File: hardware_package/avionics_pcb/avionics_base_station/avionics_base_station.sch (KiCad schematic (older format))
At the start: 3 parts, among them U1 NODEMCU, U2 RFM98

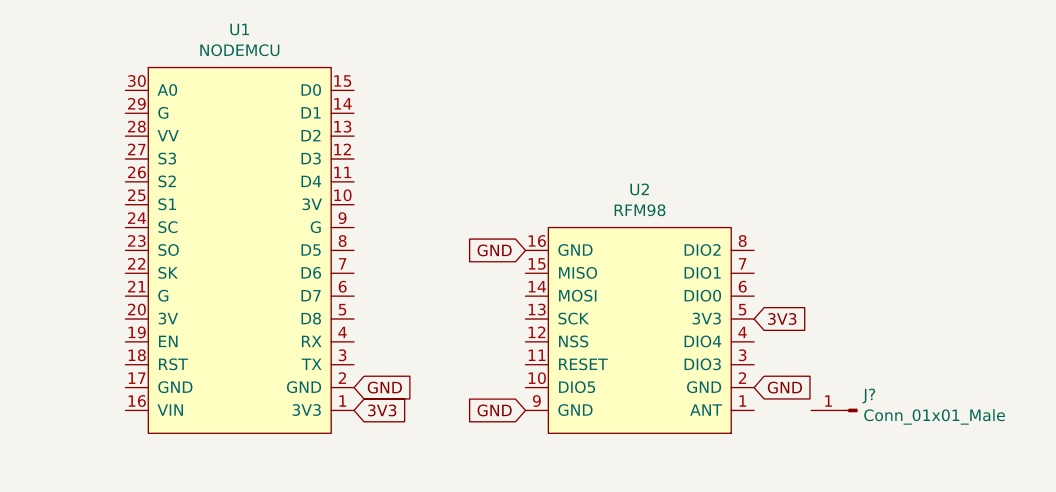
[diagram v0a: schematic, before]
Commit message: Completed the base station PCB
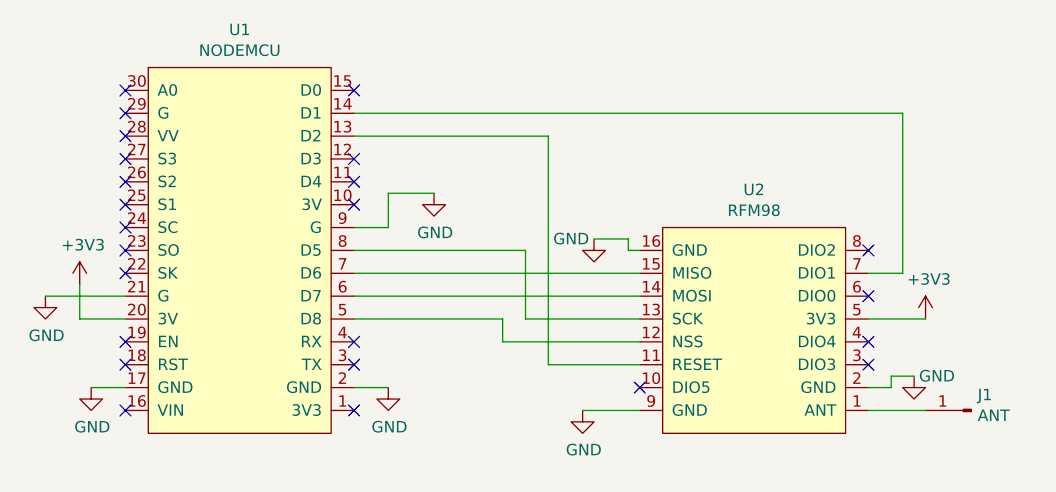
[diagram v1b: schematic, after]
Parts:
- J1: renamed from J?; value Conn_01x01_Male -> ANT; footprint (none) -> Connector_Wire:SolderWire-0.1sqmm_1x01_D0.4mm_OD1mm
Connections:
- net GND: now also U1.17 (GND), U1.21 (G), U1.9 (G)
- net at U1.13 (D2): now also U2.11 (RESET)
- net at U1.14 (D1): now also U2.7 (DIO1)
- net +3V3: now reaches U1.20 (3V)
- net +3V3: now also U2.5 (3V3)
- net at U1.5 (D8): now also U2.12 (NSS)
- net at U1.6 (D7): now also U2.14 (MOSI)
- net at U1.7 (D6): now also U2.15 (MISO)
- net at U1.8 (D5): now also U2.13 (SCK)
- net at U2.1 (ANT): now also J1.1 (Pin_1)
- net 3V3: no longer names the net of U1.1 (3V3)
- net 3V3: no longer U2.5 (3V3)
- no-connect marks 0 -> 24
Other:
- moved on the sheet: J1, U2
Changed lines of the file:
@@
 L avionics:RFM98 U2
 U 1 1 5F65755F
-P 3800 2450
-F 0 "U2" H 3800 3065 50  0000 C CNN
-F 1 "RFM98" H 3800 2974 50  0000 C CNN
-F 2 "avionics:RFM98" H 3800 1900 50  0001 C CNN
-F 3 "" H 3800 2450 50  0001 C CNN
-	1    3800 2450
-	1    0    0    -1
-$EndComp
-Text GLabel 2550 2800 2    50   Input ~ 0
-3V3
-Text GLabel 4300 2400 2    50   Input ~ 0
-3V3
-Text GLabel 2550 2700 2    50   Input ~ 0
-GND
-Text GLabel 4300 2700 2    50   Input ~ 0
-GND
-Text GLabel 3300 2100 0    50   Input ~ 0
-GND
-Text GLabel 3300 2800 0    50   Input ~ 0
-GND
-$Comp
-L Connector:Conn_01x01_Male J?
+P 4300 2450
+F 0 "U2" H 4300 3065 50  0000 C CNN
+F 1 "RFM98" H 4300 2974 50  0000 C CNN
+F 2 "avionics:RFM98" H 4300 1900 50  0001 C CNN
+F 3 "" H 4300 2450 50  0001 C CNN
+	1    4300 2450
+	1    0    0    -1
+$EndComp
+Wire Wire Line
+	4800 2800 5050 2800
+Wire Wire Line
+	2550 1500 4950 1500
+Wire Wire Line
+	4950 2200 4800 2200
+Wire Wire Line
+	2550 2300 3800 2300
+Wire Wire Line
+	3800 2200 2550 2200
+Wire Wire Line
+	2550 2100 3300 2100
+Wire Wire Line
+	3300 2100 3300 2400
+Wire Wire Line
+	3300 2400 3800 2400
+Wire Wire Line
+	3800 2500 3200 2500
+Wire Wire Line
+	3200 2500 3200 2400
+Wire Wire Line
+	2550 2400 3200 2400
+Wire Wire Line
+	3800 2600 3400 2600
+Wire Wire Line
+	3400 2600 3400 1600
+Wire Wire Line
+	2550 1600 3400 1600
+Wire Wire Line
+	4950 1500 4950 2200
+NoConn ~ 4800 2100
+NoConn ~ 4800 2300
+NoConn ~ 4800 2500
+NoConn ~ 4800 2600
+NoConn ~ 3800 2700
+NoConn ~ 2550 1400
+NoConn ~ 2550 1700
+NoConn ~ 2550 1800
+NoConn ~ 2550 1900
+NoConn ~ 2550 2500
+NoConn ~ 2550 2600
+NoConn ~ 1550 1400
+NoConn ~ 1550 1500
+NoConn ~ 1550 1600
+NoConn ~ 1550 1700
+NoConn ~ 1550 1800
+NoConn ~ 1550 1900
+NoConn ~ 1550 2000
+NoConn ~ 1550 2100
+NoConn ~ 1550 2200
+NoConn ~ 1550 2500
+NoConn ~ 1550 2600
+NoConn ~ 1550 2800
+NoConn ~ 2550 2800
+$Comp
+L Connector:Conn_01x01_Male J1
 U 1 1 5F65C25B
-P 4750 2800
-F 0 "J?" H 4722 2732 50  0000 R CNN
-F 1 "Conn_01x01_Male" H 4722 2823 50  0000 R CNN
-F 2 "" H 4750 2800 50  0001 C CNN
-F 3 "~" H 4750 2800 50  0001 C CNN
-	1    4750 2800
+P 5250 2800
+F 0 "J1" H 5222 2732 50  0000 R CNN
+F 1 "ANT" H 5222 2823 50  0000 R CNN
+F 2 "Connector_Wire:SolderWire-0.1sqmm_1x01_D0.4mm_OD1mm" H 5250 2800 50  0001 C CNN
+F 3 "~" H 5250 2800 50  0001 C CNN
+	1    5250 2800
 	-1   0    0    1
 $EndComp
+$Comp
+L power:GND #PWR0101
+U 1 1 5F66EE28
+P 2700 2700
+F 0 "#PWR0101" H 2700 2450 50  0001 C CNN
+F 1 "GND" H 2705 2527 50  0000 C CNN
+F 2 "" H 2700 2700 50  0001 C CNN
+F 3 "" H 2700 2700 50  0001 C CNN
+	1    2700 2700
+	1    0    0    -1
+$EndComp
+$Comp
+L power:GND #PWR0102
+U 1 1 5F66FA24
+P 1400 2700
+F 0 "#PWR0102" H 1400 2450 50  0001 C CNN
+F 1 "GND" H 1405 2527 50  0000 C CNN
+F 2 "" H 1400 2700 50  0001 C CNN
+F 3 "" H 1400 2700 50  0001 C CNN
+	1    1400 2700
+	1    0    0    -1
+$EndComp
+$Comp
+L power:GND #PWR0103
+U 1 1 5F670779
+P 2900 1850
+F 0 "#PWR0103" H 2900 1600 50  0001 C CNN
+F 1 "GND" H 2905 1677 50  0000 C CNN
+F 2 "" H 2900 1850 50  0001 C CNN
+F 3 "" H 2900 1850 50  0001 C CNN
+	1    2900 1850
+	1    0    0    -1
+$EndComp
+$Comp
+L power:GND #PWR0104
+U 1 1 5F671381
+P 1200 2300
+F 0 "#PWR0104" H 1200 2050 50  0001 C CNN
+F 1 "GND" H 1205 2127 50  0000 C CNN
+F 2 "" H 1200 2300 50  0001 C CNN
+F 3 "" H 1200 2300 50  0001 C CNN
+	1    1200 2300
+	1    0    0    -1
+$EndComp
+Wire Wire Line
+	1550 2300 1200 2300
+Wire Wire Line
+	1550 2700 1400 2700
+Wire Wire Line
+	2550 2700 2700 2700
+Wire Wire Line
+	2900 1850 2700 1850
+Wire Wire Line
+	2700 1850 2700 2000
+Wire Wire Line
+	2700 2000 2550 2000
+$Comp
+L power:GND #PWR0105
+U 1 1 5F672821
+P 3550 2800
+F 0 "#PWR0105" H 3550 2550 50  0001 C CNN
+F 1 "GND" H 3555 2627 50  0000 C CNN
+F 2 "" H 3550 2800 50  0001 C CNN
+F 3 "" H 3550 2800 50  0001 C CNN
+	1    3550 2800
+	1    0    0    -1
+$EndComp
+$Comp
+L power:GND #PWR0106
+U 1 1 5F673498
+P 5000 2650
+F 0 "#PWR0106" H 5000 2400 50  0001 C CNN
+F 1 "GND" H 5100 2650 50  0000 C CNN
+F 2 "" H 5000 2650 50  0001 C CNN
+F 3 "" H 5000 2650 50  0001 C CNN
+	1    5000 2650
+	1    0    0    -1
+$EndComp
+Wire Wire Line
+	4800 2700 4900 2700
+Wire Wire Line
+	4900 2700 4900 2650
+Wire Wire Line
+	4900 2650 5000 2650
+$Comp
+L power:GND #PWR0107
+U 1 1 5F674370
+P 3600 2050
+F 0 "#PWR0107" H 3600 1800 50  0001 C CNN
+F 1 "GND" H 3500 2050 50  0000 C CNN
+F 2 "" H 3600 2050 50  0001 C CNN
+F 3 "" H 3600 2050 50  0001 C CNN
+	1    3600 2050
+	1    0    0    -1
+$EndComp
+Wire Wire Line
+	3600 2050 3750 2050
+Wire Wire Line
+	3750 2050 3750 2100
+Wire Wire Line
+	3750 2100 3800 2100
+$Comp
+L power:+3V3 #PWR0108
+U 1 1 5F6768FE
+P 5050 2400
+F 0 "#PWR0108" H 5050 2250 50  0001 C CNN
+F 1 "+3V3" H 5065 2573 50  0000 C CNN
+F 2 "" H 5050 2400 50  0001 C CNN
+F 3 "" H 5050 2400 50  0001 C CNN
+	1    5050 2400
+	1    0    0    -1
+$EndComp
+Wire Wire Line
+	4800 2400 5050 2400
+$Comp
+L power:+3V3 #PWR0109
+U 1 1 5F677986
+P 1350 2250
+F 0 "#PWR0109" H 1350 2100 50  0001 C CNN
+F 1 "+3V3" H 1365 2423 50  0000 C CNN
+F 2 "" H 1350 2250 50  0001 C CNN
+F 3 "" H 1350 2250 50  0001 C CNN
+	1    1350 2250
+	1    0    0    -1
+$EndComp
+Wire Wire Line
+	1350 2250 1350 2400
+Wire Wire Line
+	1350 2400 1550 2400
+Wire Wire Line
+	3550 2800 3800 2800
 $EndSCHEMATC

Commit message: Refactored the PCB and schematic to be placed in a readme. Also created a readme for the Base Station PCB, and added the images
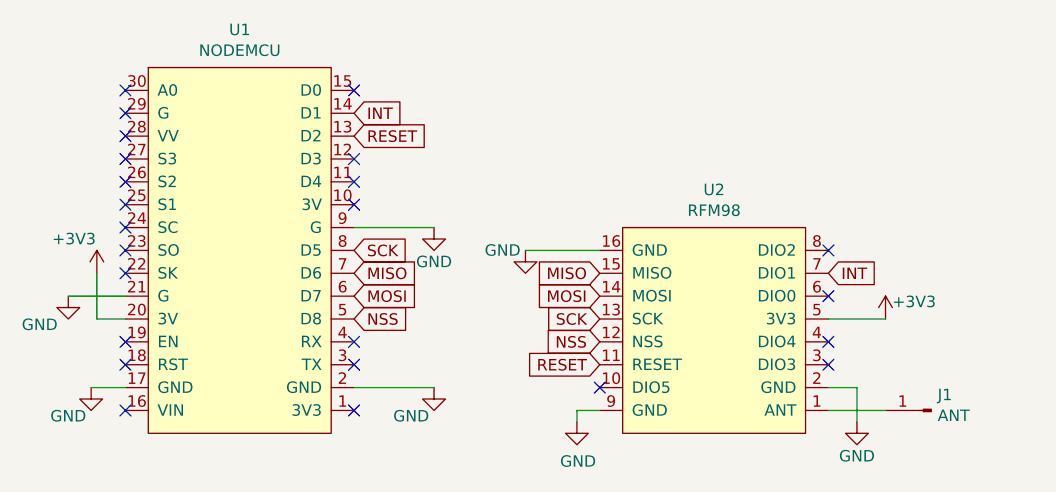
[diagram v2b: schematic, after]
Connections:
- net RESET: now reaches U1.13 (D2), U2.11 (RESET)
- net INT: now reaches U1.14 (D1), U2.7 (DIO1)
- net NSS: now reaches U1.5 (D8), U2.12 (NSS)
- net MOSI: now reaches U1.6 (D7), U2.14 (MOSI)
- net MISO: now reaches U1.7 (D6), U2.15 (MISO)
- net SCK: now reaches U1.8 (D5), U2.13 (SCK)
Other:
- moved on the sheet: J1, U2
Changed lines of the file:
@@
 L avionics:RFM98 U2
 U 1 1 5F65755F
-P 4300 2450
-F 0 "U2" H 4300 3065 50  0000 C CNN
-F 1 "RFM98" H 4300 2974 50  0000 C CNN
-F 2 "avionics:RFM98" H 4300 1900 50  0001 C CNN
-F 3 "" H 4300 2450 50  0001 C CNN
-	1    4300 2450
+P 4125 2450
+F 0 "U2" H 4125 3065 50  0000 C CNN
+F 1 "RFM98" H 4125 2974 50  0000 C CNN
+F 2 "avionics:RFM98" H 4125 1900 50  0001 C CNN
+F 3 "" H 4125 2450 50  0001 C CNN
+	1    4125 2450
 	1    0    0    -1
 $EndComp
 Wire Wire Line
-	4800 2800 5050 2800
-Wire Wire Line
-	2550 1500 4950 1500
-Wire Wire Line
-	4950 2200 4800 2200
-Wire Wire Line
-	2550 2300 3800 2300
-Wire Wire Line
-	3800 2200 2550 2200
-Wire Wire Line
-	2550 2100 3300 2100
-Wire Wire Line
-	3300 2100 3300 2400
-Wire Wire Line
-	3300 2400 3800 2400
-Wire Wire Line
-	3800 2500 3200 2500
-Wire Wire Line
-	3200 2500 3200 2400
-Wire Wire Line
-	2550 2400 3200 2400
-Wire Wire Line
-	3800 2600 3400 2600
-Wire Wire Line
-	3400 2600 3400 1600
-Wire Wire Line
-	2550 1600 3400 1600
-Wire Wire Line
-	4950 1500 4950 2200
-NoConn ~ 4800 2100
-NoConn ~ 4800 2300
-NoConn ~ 4800 2500
-NoConn ~ 4800 2600
-NoConn ~ 3800 2700
+	4625 2800 4875 2800
+NoConn ~ 4625 2100
+NoConn ~ 4625 2300
+NoConn ~ 4625 2500
+NoConn ~ 4625 2600
+NoConn ~ 3625 2700
 NoConn ~ 2550 1400
 NoConn ~ 2550 1700
@@
 L Connector:Conn_01x01_Male J1
 U 1 1 5F65C25B
-P 5250 2800
-F 0 "J1" H 5222 2732 50  0000 R CNN
-F 1 "ANT" H 5222 2823 50  0000 R CNN
-F 2 "Connector_Wire:SolderWire-0.1sqmm_1x01_D0.4mm_OD1mm" H 5250 2800 50  0001 C CNN
-F 3 "~" H 5250 2800 50  0001 C CNN
-	1    5250 2800
+P 5075 2800
+F 0 "J1" H 5047 2732 50  0000 R CNN
+F 1 "ANT" H 5047 2823 50  0000 R CNN
+F 2 "Connector_Wire:SolderWire-0.1sqmm_1x01_D0.4mm_OD1mm" H 5075 2800 50  0001 C CNN
+F 3 "~" H 5075 2800 50  0001 C CNN
+	1    5075 2800
 	-1   0    0    1
 $EndComp
@@
 L power:GND #PWR0101
 U 1 1 5F66EE28
-P 2700 2700
-F 0 "#PWR0101" H 2700 2450 50  0001 C CNN
-F 1 "GND" H 2705 2527 50  0000 C CNN
-F 2 "" H 2700 2700 50  0001 C CNN
-F 3 "" H 2700 2700 50  0001 C CNN
-	1    2700 2700
+P 2900 2700
+F 0 "#PWR0101" H 2900 2450 50  0001 C CNN
+F 1 "GND" H 2800 2575 50  0000 C CNN
+F 2 "" H 2900 2700 50  0001 C CNN
+F 3 "" H 2900 2700 50  0001 C CNN
+	1    2900 2700
 	1    0    0    -1
 $EndComp
@@
 P 1400 2700
 F 0 "#PWR0102" H 1400 2450 50  0001 C CNN
-F 1 "GND" H 1405 2527 50  0000 C CNN
+F 1 "GND" H 1300 2575 50  0000 C CNN
 F 2 "" H 1400 2700 50  0001 C CNN
 F 3 "" H 1400 2700 50  0001 C CNN
@@
 L power:GND #PWR0103
 U 1 1 5F670779
-P 2900 1850
-F 0 "#PWR0103" H 2900 1600 50  0001 C CNN
-F 1 "GND" H 2905 1677 50  0000 C CNN
-F 2 "" H 2900 1850 50  0001 C CNN
-F 3 "" H 2900 1850 50  0001 C CNN
-	1    2900 1850
+P 2900 2000
+F 0 "#PWR0103" H 2900 1750 50  0001 C CNN
+F 1 "GND" H 2900 1850 50  0000 C CNN
+F 2 "" H 2900 2000 50  0001 C CNN
+F 3 "" H 2900 2000 50  0001 C CNN
+	1    2900 2000
 	1    0    0    -1
 $EndComp
@@
 L power:GND #PWR0104
 U 1 1 5F671381
-P 1200 2300
-F 0 "#PWR0104" H 1200 2050 50  0001 C CNN
-F 1 "GND" H 1205 2127 50  0000 C CNN
-F 2 "" H 1200 2300 50  0001 C CNN
-F 3 "" H 1200 2300 50  0001 C CNN
-	1    1200 2300
+P 1300 2300
+F 0 "#PWR0104" H 1300 2050 50  0001 C CNN
+F 1 "GND" H 1175 2175 50  0000 C CNN
+F 2 "" H 1300 2300 50  0001 C CNN
+F 3 "" H 1300 2300 50  0001 C CNN
+	1    1300 2300
 	1    0    0    -1
 $EndComp
 Wire Wire Line
-	1550 2300 1200 2300
-Wire Wire Line
 	1550 2700 1400 2700
-Wire Wire Line
-	2550 2700 2700 2700
-Wire Wire Line
-	2900 1850 2700 1850
-Wire Wire Line
-	2700 1850 2700 2000
-Wire Wire Line
-	2700 2000 2550 2000
 $Comp
 L power:GND #PWR0105
 U 1 1 5F672821
-P 3550 2800
-F 0 "#PWR0105" H 3550 2550 50  0001 C CNN
-F 1 "GND" H 3555 2627 50  0000 C CNN
-F 2 "" H 3550 2800 50  0001 C CNN
-F 3 "" H 3550 2800 50  0001 C CNN
-	1    3550 2800
+P 3525 2850
+F 0 "#PWR0105" H 3525 2600 50  0001 C CNN
+F 1 "GND" H 3530 2677 50  0000 C CNN
+F 2 "" H 3525 2850 50  0001 C CNN
+F 3 "" H 3525 2850 50  0001 C CNN
+	1    3525 2850
 	1    0    0    -1
 $EndComp
@@
 L power:GND #PWR0106
 U 1 1 5F673498
-P 5000 2650
-F 0 "#PWR0106" H 5000 2400 50  0001 C CNN
-F 1 "GND" H 5100 2650 50  0000 C CNN
-F 2 "" H 5000 2650 50  0001 C CNN
-F 3 "" H 5000 2650 50  0001 C CNN
-	1    5000 2650
+P 4750 2850
+F 0 "#PWR0106" H 4750 2600 50  0001 C CNN
+F 1 "GND" H 4750 2700 50  0000 C CNN
+F 2 "" H 4750 2850 50  0001 C CNN
+F 3 "" H 4750 2850 50  0001 C CNN
+	1    4750 2850
+	1    0    0    -1
+$EndComp
+$Comp
+L power:GND #PWR0107
+U 1 1 5F674370
+P 3300 2100
+F 0 "#PWR0107" H 3300 1850 50  0001 C CNN
+F 1 "GND" H 3200 2100 50  0000 C CNN
+F 2 "" H 3300 2100 50  0001 C CNN
+F 3 "" H 3300 2100 50  0001 C CNN
+	1    3300 2100
+	1    0    0    -1
+$EndComp
+$Comp
+L power:+3V3 #PWR0108
+U 1 1 5F6768FE
+P 4875 2400
+F 0 "#PWR0108" H 4875 2250 50  0001 C CNN
+F 1 "+3V3" H 5000 2475 50  0000 C CNN
+F 2 "" H 4875 2400 50  0001 C CNN
+F 3 "" H 4875 2400 50  0001 C CNN
+	1    4875 2400
 	1    0    0    -1
 $EndComp
 Wire Wire Line
-	4800 2700 4900 2700
-Wire Wire Line
-	4900 2700 4900 2650
-Wire Wire Line
-	4900 2650 5000 2650
-$Comp
-L power:GND #PWR0107
-U 1 1 5F674370
-P 3600 2050
-F 0 "#PWR0107" H 3600 1800 50  0001 C CNN
-F 1 "GND" H 3500 2050 50  0000 C CNN
-F 2 "" H 3600 2050 50  0001 C CNN
-F 3 "" H 3600 2050 50  0001 C CNN
-	1    3600 2050
-	1    0    0    -1
-$EndComp
-Wire Wire Line
-	3600 2050 3750 2050
-Wire Wire Line
-	3750 2050 3750 2100
-Wire Wire Line
-	3750 2100 3800 2100
-$Comp
-L power:+3V3 #PWR0108
-U 1 1 5F6768FE
-P 5050 2400
-F 0 "#PWR0108" H 5050 2250 50  0001 C CNN
-F 1 "+3V3" H 5065 2573 50  0000 C CNN
-F 2 "" H 5050 2400 50  0001 C CNN
-F 3 "" H 5050 2400 50  0001 C CNN
-	1    5050 2400
-	1    0    0    -1
-$EndComp
-Wire Wire Line
-	4800 2400 5050 2400
+	4625 2400 4875 2400
 $Comp
 L power:+3V3 #PWR0109
 U 1 1 5F677986
-P 1350 2250
-F 0 "#PWR0109" H 1350 2100 50  0001 C CNN
-F 1 "+3V3" H 1365 2423 50  0000 C CNN
-F 2 "" H 1350 2250 50  0001 C CNN
-F 3 "" H 1350 2250 50  0001 C CNN
-	1    1350 2250
+P 1425 2200
+F 0 "#PWR0109" H 1425 2050 50  0001 C CNN
+F 1 "+3V3" H 1325 2350 50  0000 C CNN
+F 2 "" H 1425 2200 50  0001 C CNN
+F 3 "" H 1425 2200 50  0001 C CNN
+	1    1425 2200
 	1    0    0    -1
 $EndComp
+Text GLabel 4625 2200 2    50   Input ~ 0
+INT
+Text GLabel 2550 1500 2    50   Input ~ 0
+INT
+Text GLabel 2550 1600 2    50   Input ~ 0
+RESET
+Text GLabel 3625 2600 0    50   Input ~ 0
+RESET
 Wire Wire Line
-	1350 2250 1350 2400
+	3625 2800 3525 2800
 Wire Wire Line
-	1350 2400 1550 2400
+	3525 2800 3525 2850
 Wire Wire Line
-	3550 2800 3800 2800
+	4625 2700 4750 2700
+Wire Wire Line
+	4750 2700 4750 2850
+Text GLabel 2550 2400 2    50   Input ~ 0
+NSS
+Text GLabel 3625 2500 0    50   Input ~ 0
+NSS
+Text GLabel 2550 2100 2    50   Input ~ 0
+SCK
+Text GLabel 3625 2400 0    50   Input ~ 0
+SCK
+Text GLabel 2550 2200 2    50   Input ~ 0
+MISO
+Text GLabel 3625 2200 0    50   Input ~ 0
+MISO
+Text GLabel 2550 2300 2    50   Input ~ 0
+MOSI
+Text GLabel 3625 2300 0    50   Input ~ 0
+MOSI
+Wire Wire Line
+	3300 2100 3625 2100
+Wire Wire Line
+	2550 2000 2900 2000
+Wire Wire Line
+	2550 2700 2900 2700
+Wire Wire Line
+	1550 2300 1300 2300
+Wire Wire Line
+	1425 2200 1425 2400
+Wire Wire Line
+	1425 2400 1550 2400
 $EndSCHEMATC
